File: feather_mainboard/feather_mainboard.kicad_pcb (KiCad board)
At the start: 2 copper layers, 60 x 60 mm, 42 parts, among them J1 62501021721, J2 62501021721, J3 61300211121, J4 693071020811, J5 61300211121, J6 61300211121, J7 61300211121, J8 61300211121, U1 Adafruit ESP32-S3 Feather, U2 SI2307CDS-T1-BE3, U3 2N7002K-T1-GE3, U4 WPME-FISM_SMT-8

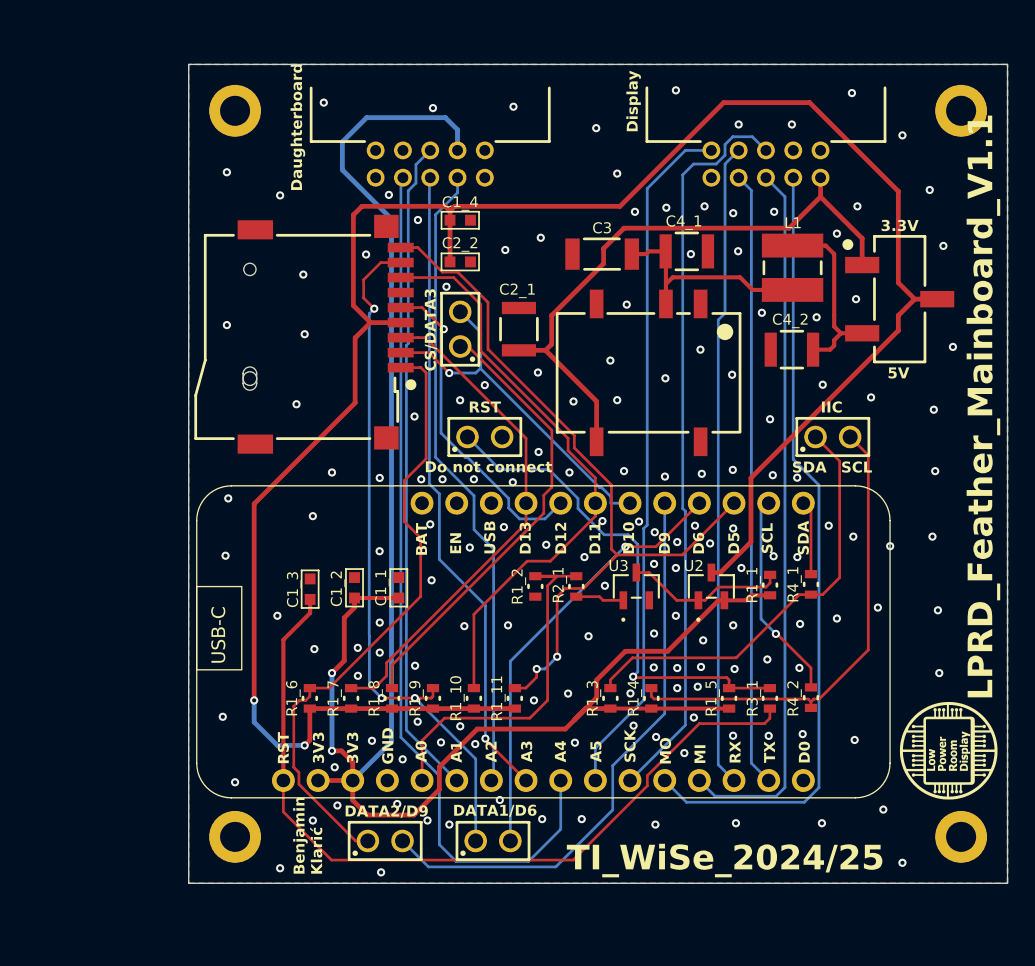
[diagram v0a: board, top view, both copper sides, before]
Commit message: Updated the mainboard: removed unnecessary pull-ups on SD card lines; connected IIC pull-ups to enable circuit; cleaned up schematic
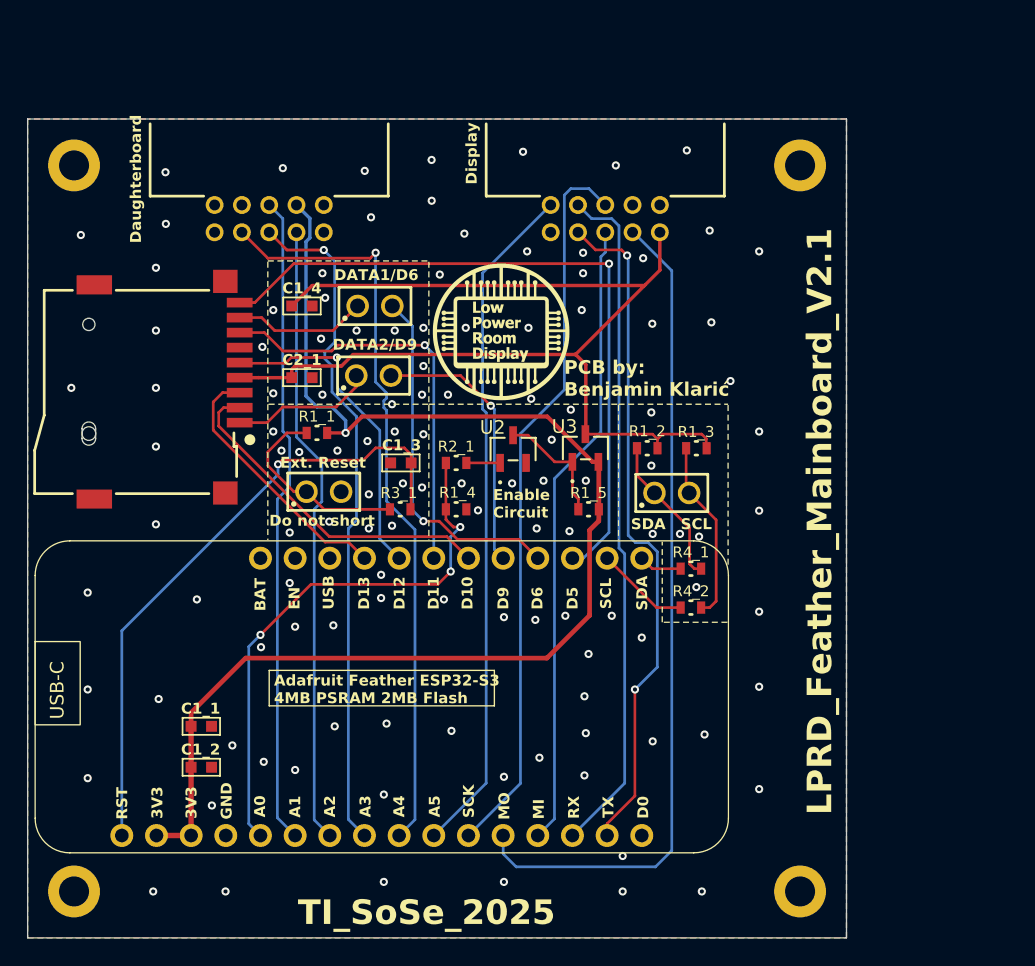
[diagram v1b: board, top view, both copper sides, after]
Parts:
- removed C2_2: 10µF, Custom footprints:WCAP-CSGP_0603_R
- removed C3: 470pF, Custom footprints:WCAP-CSMH_1808_H2.0
- removed C4_1, C4_2: 4.7µF, Custom footprints:WCAP-CSGP_1210_H2.0
- removed J8: 61300211121, Custom footprints:61300211121
- removed L1: 6.8µH, Custom footprints:WE-PD2_4532
- removed R1_10, R1_11, R1_6, R1_7, R1_8, R1_9: 10kΩ, Custom footprints:WRIS-RSKS_0603_REFLOW
- removed S1: 450406020024, Custom footprints:450406020024
- removed U4: WPME-FISM_SMT-8, Custom footprints:WPME-FISM_SMT-8_L13.2W11.4H7.25
- C2_1: footprint Custom footprints:WCAP-CSGP_1210_H2.0 -> Custom footprints:WCAP-CSGP_0603_R
- J1, J2: value 62501021721 -> 61300211121; footprint Custom footprints:62501021721 -> Custom footprints:61300211121
- J3, J7: value 61300211121 -> 62501021721; footprint Custom footprints:61300211121 -> Custom footprints:62501021721_full
- J4: value 693071020811 -> 61300211121; footprint Custom footprints:693071020811 -> Custom footprints:61300211121
- J6: value 61300211121 -> 693071020811; footprint Custom footprints:61300211121 -> Custom footprints:693071020811
- U2: value SI2307CDS-T1-BE3 -> 2N7002K-T1-GE3; footprint Custom footprints:SOT-23_VIS -> Custom footprints:SOT_02K-T1-GE3_VIS
- U3: value 2N7002K-T1-GE3 -> SI2307CDS-T1-BE3; footprint Custom footprints:SOT_02K-T1-GE3_VIS -> Custom footprints:SOT-23_VIS
- moved H3 65.1 mm to (111.4, 130.0)
- moved J6 54.6 mm to (112.5, 93.4), turned to -90 degrees
- moved J7 50.9 mm to (125.7, 76.2), turned to 180 degrees
- moved J1 43.2 mm to (129.7, 100.7), turned to 0 degrees
- moved H4 41.6 mm to (164.6, 130.0)
- moved R1_1 35.0 mm to (129.2, 96.4), turned to 0 degrees
- moved J2 33.7 mm to (155.2, 100.8), turned to 0 degrees
- moved R3_1 30.4 mm to (135.3, 102.0), turned to 180 degrees
- moved J3 22.4 mm to (150.3, 76.2), turned to 180 degrees
- moved R1_4 19.9 mm to (139.4, 102.0), turned to 180 degrees
- moved R1_3 19.4 mm to (157.0, 97.5), turned to 0 degrees
- moved C1_1 17.7 mm to (120.7, 117.9), turned to 0 degrees
- moved U2 17.7 mm to (143.6, 97.6)
- moved C1_2 17.3 mm to (120.7, 120.9), turned to 0 degrees
- moved R1_5 17.3 mm to (149.1, 102.0), turned to 0 degrees
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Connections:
- net /IIC/SCL renamed /IIC Connector/SCL
- net /IIC/SDA renamed /IIC Connector/SDA
- C1_4 pad 2: /Display-Enable/Switch -> Enable VCC
- C2_1 pad 1: /Boost-Converter/VOUT+ -> GND
- C2_1 pad 2: GND -> Enable VCC
- J1 pad 1: unconnected-(J1-Pad1) -> Net-(J1-Pad1)
- J1 pad 2: /Display-Ports/BUSY -> GND
- J2 pad 1: unconnected-(J2-Pad1) -> Net-(J2-Pad1)
- J2 pad 2: unconnected-(J2-Pad2) -> Net-(J2-Pad2)
- J3 pad 1: Net-(J3-Pad1) -> unconnected-(J3-Pad1)
- J3 pad 2: GND -> /Display Ports/DISPLAY_BUSY
- J4 pad 1: Net-(J4-DAT2) -> Net-(J6-DAT2)
- J4 pad 2: /MicroSD-Card Adapter/SD_CS/DAT3 -> /MicroSD-Card Adapter/SD_DAT2
- J5 pad 1: Net-(J5-Pad1) -> Net-(J6-DAT1)
- J5 pad 2: /MicroSD-Card Adapter/SD_CS/DAT3 -> /MicroSD-Card Adapter/SD_DAT1
- J6 pad 1: Net-(J6-Pad1) -> Net-(J6-DAT2)
- J6 pad 2: Net-(J6-Pad2) -> /MicroSD-Card Adapter/SD_CS/DAT3
- J7 pad 1: Net-(J4-DAT2) -> unconnected-(J7-Pad1)
- J7 pad 2: /MicroSD-Card Adapter/SD_DAT2 -> unconnected-(J7-Pad2)
- R1_1 pad 1: Net-(U2-G) -> Net-(J1-Pad1)
- R1_2 pad 1: GND -> Net-(J2-Pad1)
- R1_2 pad 2: /Display-Enable/EN -> Enable VCC
- R1_3 pad 1: Net-(J6-Pad1) -> Net-(J2-Pad2)
- R1_3 pad 2: VCC -> Enable VCC
- R1_4 pad 1: Net-(J6-Pad2) -> GND
- R1_4 pad 2: VCC -> /Enable Pin/Enable Input
- R1_5 pad 1: Net-(J3-Pad1) -> Net-(U2-D)
- R2_1 pad 1: /Display-Enable/EN -> /Enable Pin/Enable Input
- R2_1 pad 2: Net-(U3-G) -> Net-(U2-G)
- R3_1 pad 2: Net-(J3-Pad1) -> Net-(J1-Pad1)
- R4_1 pad 2: Net-(J6-Pad1) -> Net-(J2-Pad1)
- R4_2 pad 2: Net-(J6-Pad2) -> Net-(J2-Pad2)
- U1 pad 10: /Display-Ports/BUSY -> /Display Ports/DISPLAY_BUSY
- U1 pad 11: /Display-Ports/SCLK -> /Display Ports/DISPLAY_SCLK
- U1 pad 12: /Display-Ports/DIN -> /Display Ports/DISPLAY_MOSI/DIN
- U1 pad 13: /Display-Ports/CS -> /Display Ports/DISPLAY_CS
- U1 pad 14: /Display-Ports/DC -> /Display Ports/DISPLAY_DC
- U1 pad 15: /Display-Ports/RST -> /Display Ports/DISPLAY_RST
- U1 pad 5: /Display-Enable/EN -> /Enable Pin/Enable Input
- U1 pad 6: /Buttons-Connector/Button_1 -> /Daughterboard Connector/Button_1
- U1 pad 7: /Buttons-Connector/Button_2 -> /Daughterboard Connector/Button_2
- U1 pad 8: /Buttons-Connector/Button_3 -> /Daughterboard Connector/Button_3
- U1 pad 9: /Buttons-Connector/Button_4 -> /Daughterboard Connector/Button_4
- U2 pad 2: VCC -> GND
- U2 pad 3: /Display-Enable/Switch -> Net-(U2-D)
- U3 pad 1: Net-(U3-G) -> Net-(U2-D)
- U3 pad 2: GND -> VCC
- U3 pad 3: Net-(U2-G) -> Enable VCC
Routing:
- net /Display-Enable/Switch: track 152.1 -> 0.00 mm, vias 2 -> 0
- net Enable VCC: track 0.00 -> 80.5 mm
- net /Buttons-Connector/Button_4: track 64.0 -> 0.00 mm
- net /Display Ports/DISPLAY_MOSI/DIN: track 0.00 -> 61.1 mm
- net /Display-Ports/DIN: track 57.9 -> 0.00 mm
- net /Daughterboard Connector/Button_4: track 0.00 -> 55.3 mm, vias 0 -> 1
- net /Display-Ports/SCLK: track 54.3 -> 0.00 mm
- net /Display Ports/DISPLAY_SCLK: track 0.00 -> 53.5 mm
- net /Display-Ports/CS: track 52.3 -> 0.00 mm
- net Net-(J4-DAT1): track 51.5 -> 0.00 mm, vias 3 -> 0
- net /Display-Ports/BUSY: track 50.8 -> 0.00 mm
- net /Display Ports/DISPLAY_DC: track 0.00 -> 50.1 mm
- net /Display Ports/DISPLAY_BUSY: track 0.00 -> 50.0 mm
- net /Display Ports/DISPLAY_RST: track 0.00 -> 49.8 mm, vias 0 -> 2
- net /Daughterboard Connector/Button_3: track 0.00 -> 49.8 mm, vias 0 -> 1
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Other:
- board text added: "Adafruit Feather ESP32-S3 4MB PSRAM 2MB Flash"
- board text added: "Do not short"
- board text added: "Enable Circuit"
- board text added: "Ext. Reset"
- board text added: "LPRD_Feather_Mainboard_V2.1"
- board text added: "PCB by: Benjamin Klarić"
- board text added: "TI_SoSe_2025"
- board text removed: "3.3V"
- board text removed: "5V"
- board text removed: "Benjamin Klarić"
- board text removed: "CS/DATA3"
- board text removed: "Do not connect"
- board text removed: "IIC"
- board text removed: "LPRD_Feather_Mainboard_V1.1"
- board text removed: "TI_WiSe_2024/25"
